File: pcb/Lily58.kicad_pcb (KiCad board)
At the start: 2 copper layers, 142.5 x 106.3 mm, 261 parts, among them P4 OLED, SW1 SW_PUSH, SW10 SW_PUSH, SW11 SW_PUSH, SW12 SW_PUSH, SW13 SW_PUSH, SW14 SW_PUSH, SW15 SW_PUSH, SW16 SW_PUSH, SW17 SW_PUSH, SW18 SW_PUSH, SW19 SW_PUSH, SW2 SW_PUSH, SW20 SW_PUSH, SW21 SW_PUSH, SW22 SW_PUSH, SW23 SW_PUSH, SW24 SW_PUSH, SW25 Rotary_Encoder_Switch, SW26 SW_PUSH, SW27 SW_PUSH, SW28 SW_PUSH, SW29 SW_PUSH, SW3 SW_PUSH, SW4 SW_PUSH, SW5 SW_PUSH, SW6 SW_PUSH, SW7 SW_PUSH, SW8 SW_PUSH, SW9 SW_PUSH, U1 NiceNano

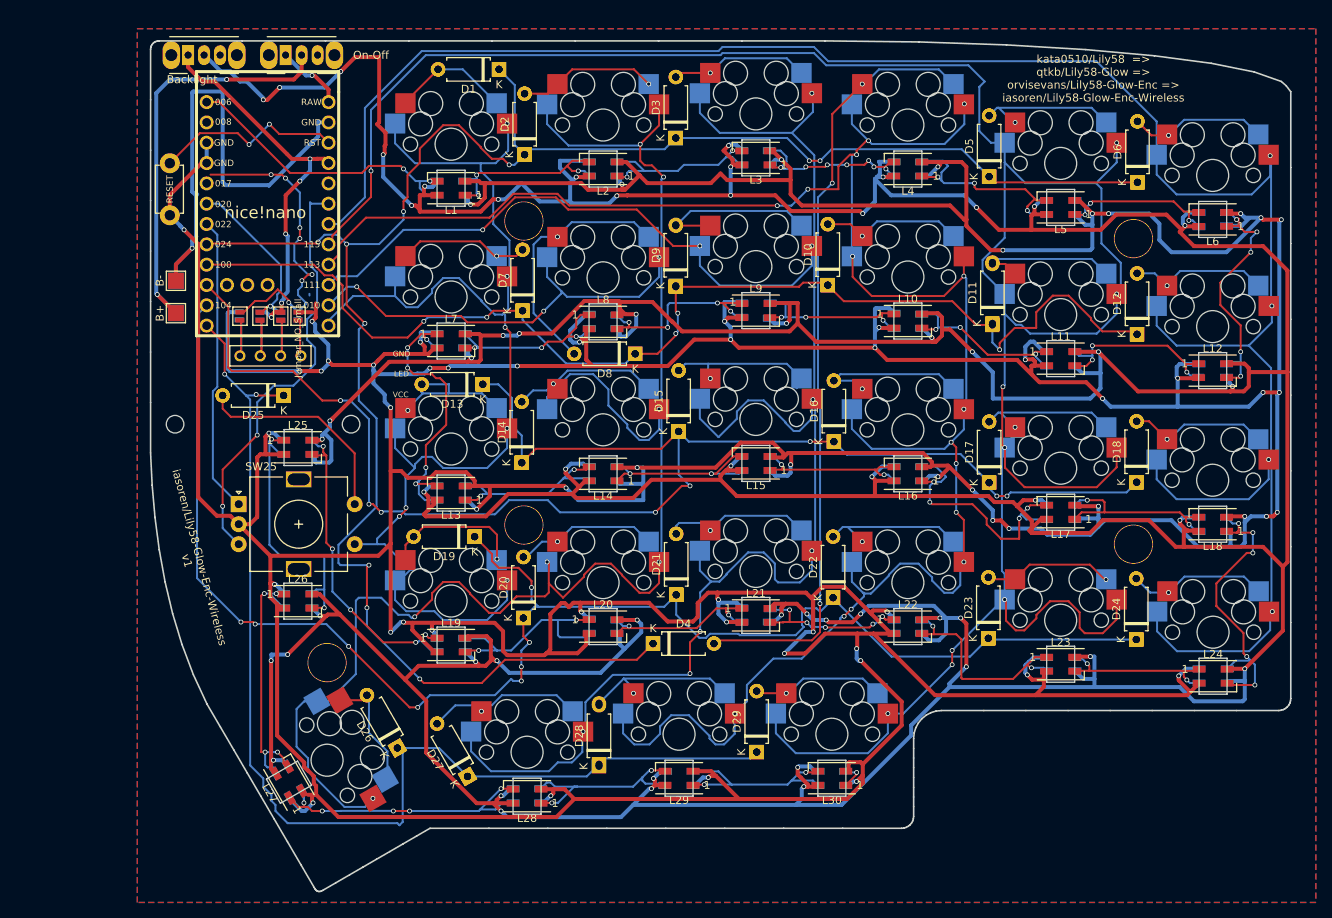
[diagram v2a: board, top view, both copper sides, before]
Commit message: Replacing V1
Starting from scratch for V1 due to some issues
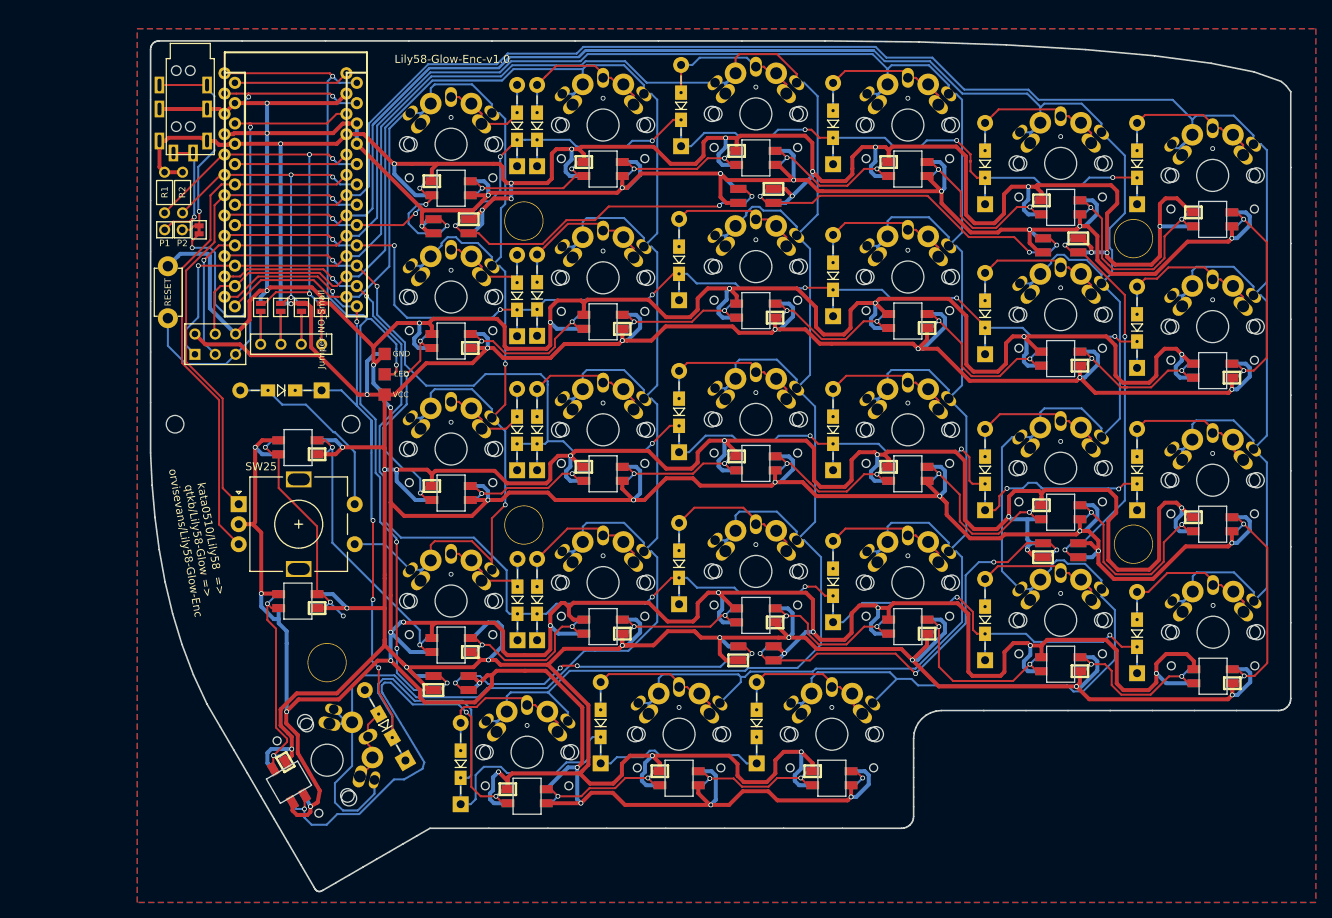
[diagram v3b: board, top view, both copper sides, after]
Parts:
- removed ? (x122): , 
- removed B+, B-: Conn_01x01_Male, TestPoint:TestPoint_Pad_2.0x2.0mm
- removed Backlight, On-Off: SW_DIP_x01, Button_Switch_THT:SW_CuK_OS102011MA1QN1_SPDT_Angled
- removed the D1 at (126.5, 40.6)
- removed the D10 at (167.6, 67.6)
- removed the D11 at (188.2, 72.4)
- removed the D12 at (206.2, 73.8)
- removed the D13 at (124.5, 80.0)
- removed the D14 at (129.3, 89.8)
- removed the D15 at (148.9, 85.9)
- removed the D16 at (168.4, 87.2)
- removed the D17 at (187.8, 92.3)
- removed the D18 at (206.2, 92.3)
- removed the D19 at (123.4, 99.1)
- removed the D2 at (129.7, 51.3)
- removed the D20 at (129.5, 109.2)
- removed the D21 at (148.6, 106.3)
- removed the D22 at (168.2, 106.7)
- removed the D23 at (187.7, 111.8)
- removed the D24 at (206.1, 111.9)
- removed the D25 at (99.6, 81.4)
- removed the D26 at (113.8, 125.5)
- removed the D27 at (122.6, 129.0)
- removed the D28 at (139.0, 127.8)
- removed the D29 at (158.7, 126.0)
- removed the D3 at (148.6, 49.2)
- removed the D4 at (145.7, 112.4)
- removed the D5 at (187.8, 54.1)
- removed the D6 at (206.3, 54.8)
- removed the D7 at (129.4, 70.8)
- removed the D8 at (143.5, 76.2)
- removed the D9 at (148.6, 67.7)
- added J1: LED, Lily58-footprint:StripLED, F.Cu at (112.2, 81.3)
- added J2: 4PIN, Lily58-footprint:MJ-4PP-9, F.Cu at (87.9, 39.3)
- added L31: SK6812mini, Lily58-footprint:SK6812MINI_underglow_rev, F.Cu at (120.5, 60.2)
- added L32: SK6812mini, Lily58-footprint:SK6812MINI_underglow_rev, F.Cu at (158.6, 56.5)
- added L33: SK6812mini, Lily58-footprint:SK6812MINI_underglow_rev, F.Cu at (196.7, 62.6)
- added L34: SK6812mini, Lily58-footprint:SK6812MINI_underglow_rev, F.Cu at (120.5, 117.3)
- added L35: SK6812mini, Lily58-footprint:SK6812MINI_underglow_rev, F.Cu at (158.6, 113.7)
- added L36: SK6812mini, Lily58-footprint:SK6812MINI_underglow_rev, F.Cu at (196.7, 100.8)
- added P1: i2c_pin, Lily58-footprint:1pin_conn, F.Cu at (84.7, 60.7)
- added P2: i2c_pin, Lily58-footprint:1pin_conn, F.Cu at (86.9, 60.7)
- added P3: ICSP, Lily58-footprint:ICSP, F.Cu at (91.0, 75.0)
- added R1: R, Lily58-footprint:RESISTOR_mini, F.Cu at (84.7, 56.0)
- added R2: R, Lily58-footprint:RESISTOR_mini, F.Cu at (86.9, 56.0)
- added W1: jumper, Lily58-footprint:jumper_data, F.Cu at (89.0, 60.7)
- D1, D10, D11, D12, D13, D14, D15, D16, D17, D18, D19, D2, D20, D21, D22, D23, D24, D25, D26, D27, D28, D29, D3, D4, D5, D6, D7, D8, D9: footprint Diode_THT:D_A-405_P7.62mm_Horizontal -> Lily58-footprint:Diode_TH_SOD123
- L1, L10, L11, L12, L13, L14, L15, L16, L17, L18, L19, L2, L20, L21, L22, L23, L24, L25, L26, L27, L28, L29, L3, L30, L4, L5, L6, L7, L8, L9: footprint LED_SMD:LED_SK6812MINI_PLCC4_3.5x3.5mm_P1.75mm -> Lily58-footprint:SK6812MINI_rev
- SW1, SW10, SW11, SW12, SW13, SW14, SW15, SW16, SW17, SW18, SW19, SW2, SW20, SW21, SW22, SW23, SW24, SW27, SW28, SW29, SW3, SW4, SW5, SW6, SW7, SW8, SW9: footprint Lily58-footprint:MX_Socket_18mm -> Lily58-footprint:MX_PG1350_FLIP_HOLES_18mm
- SW26: footprint Lily58-footprint:MX_Socket_18mm -> Lily58-footprint:MX_PG1350_FLIP_HOLES_27mm
- U1: value NiceNano -> ProMicro; footprint nice-nano-kicad:nice_nano -> Lily58-footprint:ProMicro_rev2
- moved D4 68.7 mm to (168.2, 47.5), turned to 90 degrees
- moved D8 14.2 mm to (131.3, 69.0), turned to 90 degrees
- moved RSW1 12.9 mm to (85.1, 68.5), turned to -90 degrees
- moved D19 9.58 mm to (128.8, 107.0), turned to 90 degrees
- moved D1 7.46 mm to (128.8, 47.8), turned to 90 degrees
- moved D13 7.17 mm to (128.8, 85.8), turned to 90 degrees
- moved D28 5.11 mm to (139.2, 122.4)
- moved D14 4.49 mm to (131.2, 85.8)
- moved U1 4.43 mm to (101.0, 55.9), turned to 0 degrees
- moved D3 4.03 mm to (149.2, 45.2)
- moved D2 3.88 mm to (131.2, 47.8)
- moved D21 3.84 mm to (149.0, 102.5)
- moved D29 3.58 mm to (158.7, 122.4)
- moved D9 3.34 mm to (149.0, 64.5)
- moved D26 3.15 mm to (112.3, 122.7)
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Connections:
- L1 pad 3: LEDunder -> Net-(L1-Pad3)
- L1 pad 4: Net-(L1-Pad4) -> VCC
- L10 pad 4: Net-(L1-Pad4) -> VCC
- L11 pad 4: Net-(L1-Pad4) -> VCC
- L12 pad 4: Net-(L1-Pad4) -> VCC
- L13 pad 4: Net-(L1-Pad4) -> VCC
- L14 pad 4: Net-(L1-Pad4) -> VCC
- L15 pad 4: Net-(L1-Pad4) -> VCC
- L16 pad 4: Net-(L1-Pad4) -> VCC
- L17 pad 4: Net-(L1-Pad4) -> VCC
- L18 pad 4: Net-(L1-Pad4) -> VCC
- L19 pad 4: Net-(L1-Pad4) -> VCC
- L2 pad 4: Net-(L1-Pad4) -> VCC
- L20 pad 4: Net-(L1-Pad4) -> VCC
- L21 pad 4: Net-(L1-Pad4) -> VCC
- L22 pad 4: Net-(L1-Pad4) -> VCC
- L23 pad 4: Net-(L1-Pad4) -> VCC
- L24 pad 4: Net-(L1-Pad4) -> VCC
- L25 pad 4: Net-(L1-Pad4) -> VCC
- L26 pad 4: Net-(L1-Pad4) -> VCC
- L27 pad 4: Net-(L1-Pad4) -> VCC
- L28 pad 4: Net-(L1-Pad4) -> VCC
- L29 pad 4: Net-(L1-Pad4) -> VCC
- L3 pad 4: Net-(L1-Pad4) -> VCC
- L30 pad 1: unconnected-(L30-Pad1) -> Net-(L30-Pad1)
- L30 pad 4: Net-(L1-Pad4) -> VCC
- L4 pad 4: Net-(L1-Pad4) -> VCC
- L5 pad 4: Net-(L1-Pad4) -> VCC
- L6 pad 4: Net-(L1-Pad4) -> VCC
- L7 pad 4: Net-(L1-Pad4) -> VCC
- L8 pad 4: Net-(L1-Pad4) -> VCC
- L9 pad 4: Net-(L1-Pad4) -> VCC
- SW12 pad : Net-(L12-Pad3) -> (no net)
- U1 pad 1: LEDunder -> LED
- U1 pad 2: unconnected-(U1-Pad2) -> DATA
- U1 pad 20: unconnected-(U1-Pad20) -> Net-(U1-Pad20)
- U1 pad 23: Batt- -> GND
- U1 pad 24: Batt+ -> Net-(U1-Pad24)
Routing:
- net VCC: track 49.1 -> 1045.9 mm, vias 5 -> 44
- net Net-(L1-Pad4): track 926.8 -> 0.00 mm, vias 56 -> 0
- net LED: track 0.00 -> 121.3 mm, vias 0 -> 5
- net row0: track 241.0 -> 149.6 mm, vias 10 -> 7
- net Net-(D4-Pad2): track 97.2 -> 20.0 mm, vias 3 -> 0
- net col1: track 318.6 -> 382.1 mm, vias 9 -> 0
- net Batt-: track 62.8 -> 0.00 mm, vias 1 -> 0
- net DATA: track 0.00 -> 60.9 mm, vias 0 -> 3
- net col2: track 258.3 -> 314.4 mm, vias 15 -> 1
- net Net-(L35-Pad1): track 0.00 -> 53.6 mm, vias 0 -> 4
- net Net-(J+1-Pad1): track 53.2 -> 0.00 mm, vias 2 -> 0
- net Net-(L33-Pad3): track 0.00 -> 49.9 mm, vias 0 -> 3
- net col3: track 250.6 -> 300.2 mm, vias 9 -> 1
- net Net-(L32-Pad3): track 0.00 -> 45.2 mm, vias 0 -> 3
- net Net-(L31-Pad3): track 0.00 -> 44.6 mm, vias 0 -> 3
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- added copper zone on B.Cu, net GND
- added copper zone on F.Cu, net GND
- removed copper zone on B.Cu, net SDA
- removed copper zone on F.Cu, net SDA
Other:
- rule pad_to_mask_clearance: 0 -> 0.2
- board text added: "Lily58-Glow-Enc-v1.0"
- board text added: "kata0510/Lily58 => qtkb/Lily58-Glow => orvisevans/Lily58-Glow-Enc"
- board text removed: "1"
- board text removed: "B+"
- board text removed: "B-"
- board text removed: "Backlight"
- board text removed: "L1"
- board text removed: "L10"
- board text removed: "L11"
- board text removed: "L12"
- board text removed: "L13"
- board text removed: "L14"
- board text removed: "L15"
- board text removed: "L16"
- board text removed: "L17"
- board text removed: "L18"
- board text removed: "L19"
- board text removed: "L2"
- board text removed: "L20"
- board text removed: "L21"
- board text removed: "L22"
- board text removed: "L23"
- board text removed: "L24"
- board text removed: "L25"
- board text removed: "L26"
- board text removed: "L27"
- board text removed: "L28"
- board text removed: "L29"
- board text removed: "L3"
- board text removed: "L30"
- board text removed: "L4"
- board text removed: "L5"
- board text removed: "L6"
- board text removed: "L7"
- board text removed: "L8"
- board text removed: "L9"
- board text removed: "On-Off"
- board text removed: "iasoren/Lily58-Glow-Enc-Wireless v1"
- board text removed: "kata0510/Lily58 => qtkb/Lily58-Glow => orvisevans/Lily58-Glow-Enc => iasoren/Lily58-Glow-Enc-Wireless"
